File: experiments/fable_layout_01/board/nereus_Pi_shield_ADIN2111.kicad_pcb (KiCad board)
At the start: 6 copper layers, 138 parts, among them J1 Raspberry_Pi_2_3, J5 43650-0200, T1 74930000, T2 74930000, U1 ADIN2111BCPZ, U10 LMR51430YDDCR, U11 TPS26621DRCR, U2 AP22913CN4-7, U3 AP22913CN4-7, U4 INA232AIDDFR, U5 LMR51430YDDCR, U6 TPS62840YBGR, Y1 ABM11W-25.0000MHZ-6-K1Z-T3

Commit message: fable layout 01 M0b: J5 stays the JST GH (Nick); schematic copy unchanged, board rebuilt
Co-Authored-By: Claude Fable 5.1 <noreply@anthropic.com>
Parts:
- J5: value 43650-0200 -> SM02B-GHS-TB; footprint Connector_Molex:Molex_Micro-Fit_3.0_43650-0200_1x02_P3.00mm_Horizontal -> Connector_JST:JST_GH_SM02B-GHS-TB_1x02-1MP_P1.25mm_Horizontal

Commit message: fable layout 01 M1: outline, J1, holes, inserts with Sofar's ring copper, J5, envelopes; build pipeline
Co-Authored-By: Claude Fable 5.1 <noreply@anthropic.com>
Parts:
- J1, MP1, MP2, MP3, MP4: moved to B.Cu
- moved MTG3 173.9 mm to (-3.50, 61.5)
- moved L1 167.3 mm to (12.7, 44.2), turned to 90 degrees
- moved MTG1 160.4 mm to (-3.50, 3.50)
- moved MTG4 146.0 mm to (34.5, 61.5)
- moved MP4 144.7 mm to (-1.81, 21.4), turned to 176 degrees
- moved MP3 137.2 mm to (-1.81, 12.0), turned to 176 degrees
- moved J5 136.7 mm to (15.0, 61.8)
- moved MTG2 133.8 mm to (34.5, 3.50)
- moved MP2 121.8 mm to (-1.81, 53.0), turned to 176 degrees
- moved J1 119.0 mm to (25.2, 8.37), turned to 180 degrees
- moved MP1 112.0 mm to (-1.81, 43.6), turned to 176 degrees
- moved L2 66.2 mm to (12.7, 16.8), turned to 90 degrees
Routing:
- net /Top-Level Schematic/BM2_P: track 0.00 -> 11.6 mm, vias 0 -> 7
- net /Top-Level Schematic/BM2_N: track 0.00 -> 11.6 mm, vias 0 -> 7
- net /Top-Level Schematic/BM1_P: track 0.00 -> 11.6 mm, vias 0 -> 7
- net /Top-Level Schematic/BM1_N: track 0.00 -> 11.6 mm, vias 0 -> 7
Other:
- board outline added: 46 x 65 mm
- board text added: "L1 50 W envelope 15.5 x 15.5 (+2 mm clear)"
- board text added: "L2 50 W envelope 15.5 x 15.5 (+2 mm clear)"

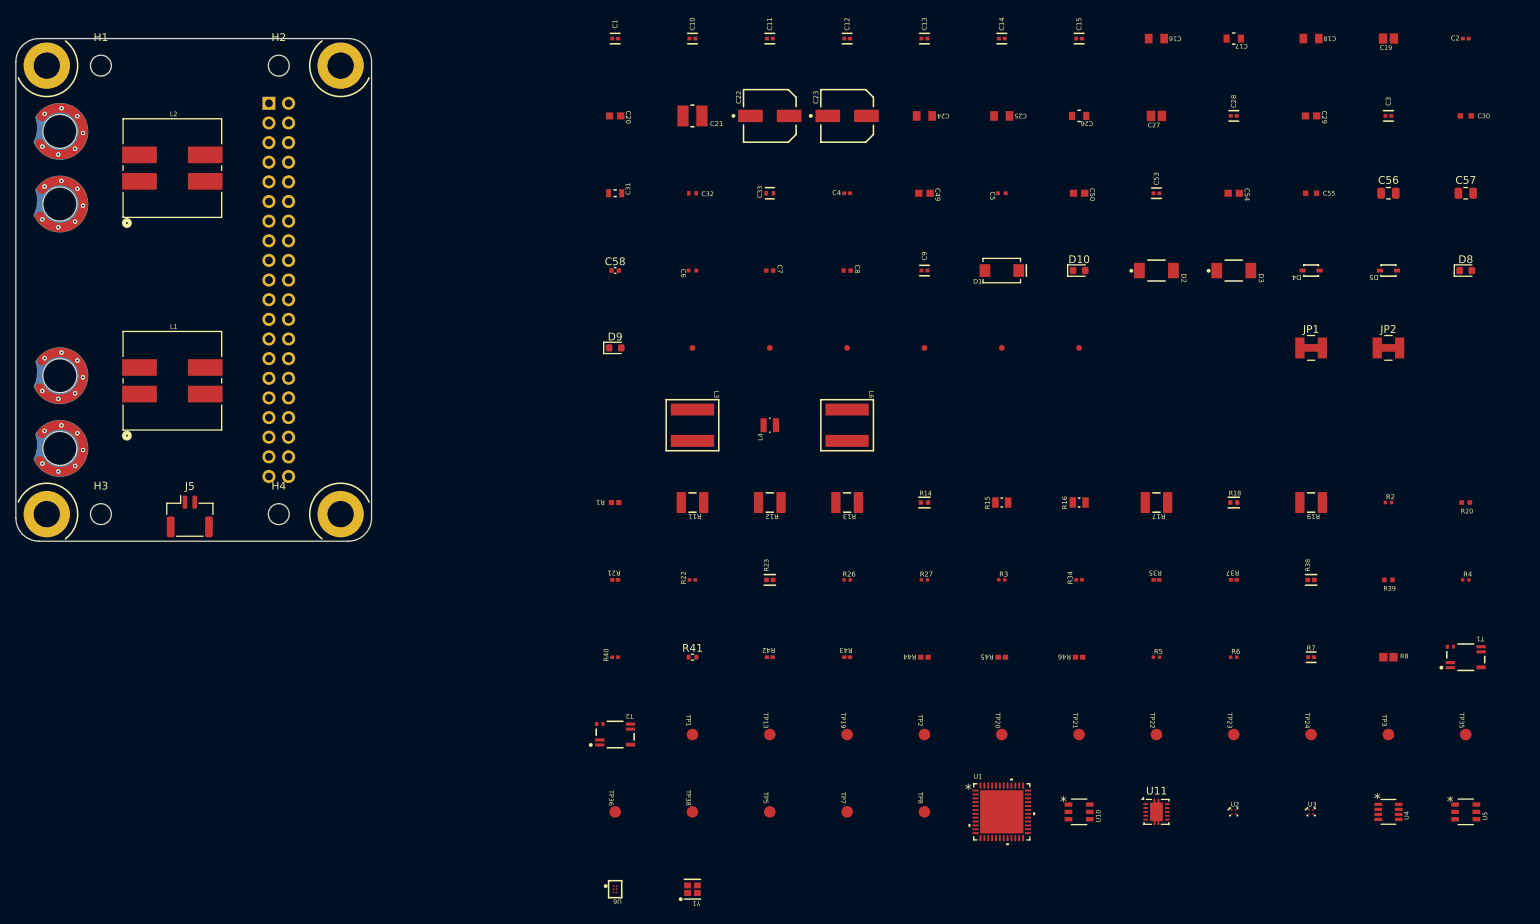
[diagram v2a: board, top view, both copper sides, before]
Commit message: fable layout 01 M2: all parts placed; rigid sub-blocks, transforms in blocks.json, heights table
Co-Authored-By: Claude Fable 5.1 <noreply@anthropic.com>
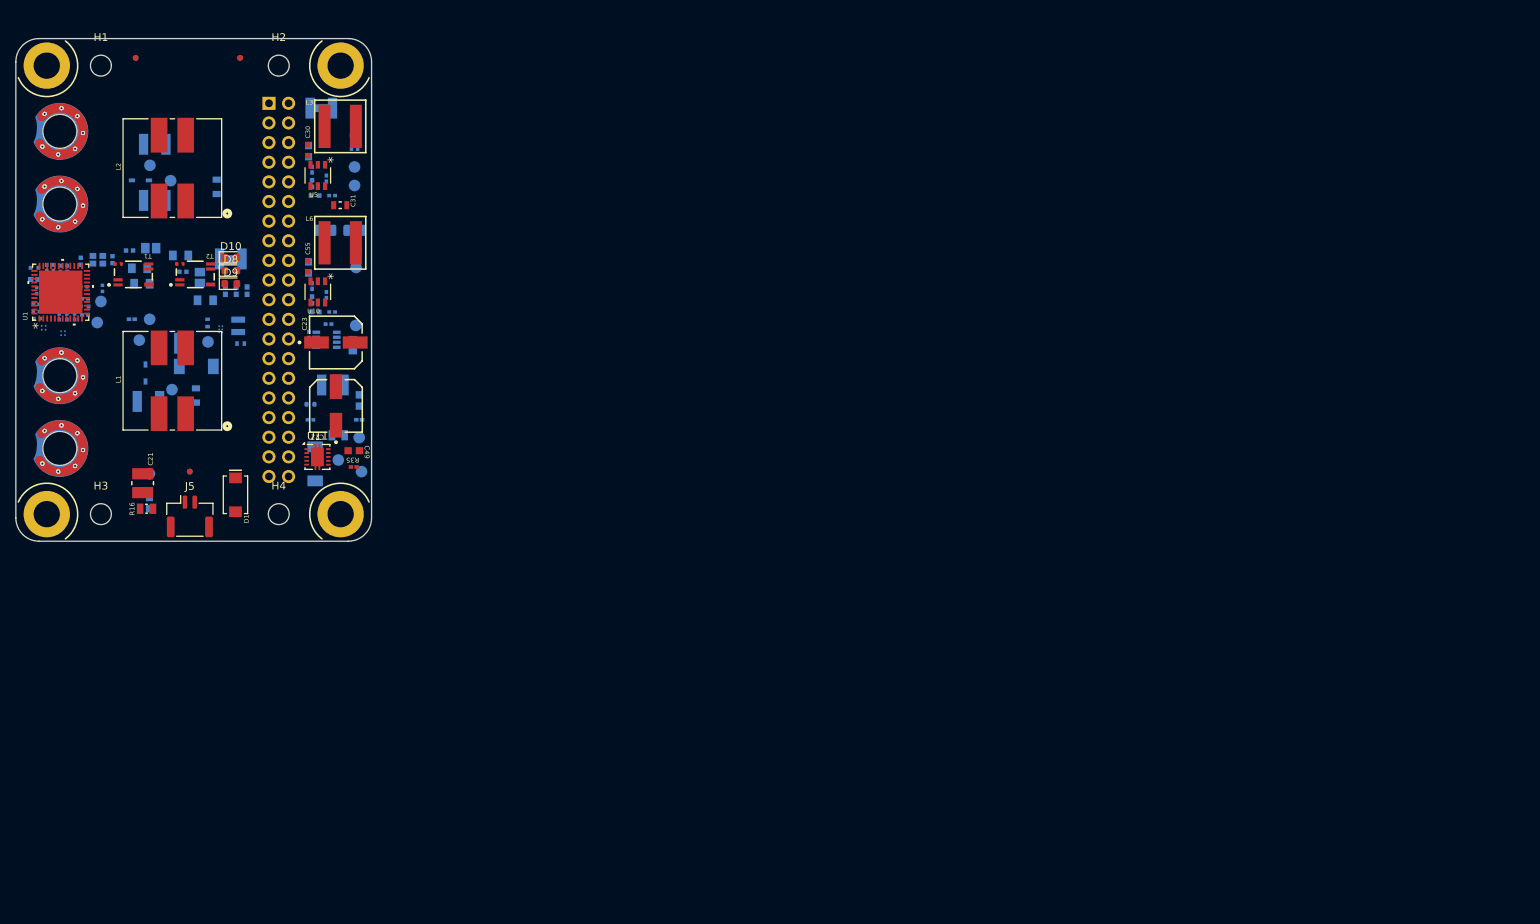
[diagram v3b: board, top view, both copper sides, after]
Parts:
- C1, C10, C11, C12, C13, C14, C15, C16, C17, C18, C19, C2, C20, C24, C25, C26, C27, C28, C29, C3, C32, C33, C4, C5, C50, C53, C54, C56, C57, C58, C6, C7, C8, C9, D2, D3, D4, D5, FID1, FID2, FID6, JP1, JP2, L4, R1, R11, R12, R13, R14, R15, R17, R18, R19, R2, R20, R21, R22, R23, R26, R27, R3, R34, R37, R38, R39, R4, R40, R41, R42, R43, R44, R45, R46, R5, R6, R7, R8, TP1, TP13, TP19, TP2, TP20, TP21, TP22, TP23, TP24, TP3, TP35, TP36, TP38, TP5, TP7, TP8, U2, U3, U4, U6, Y1: moved to B.Cu
- moved R4 188.1 mm to (-4.85, 35.3)
- moved C2 183.5 mm to (0.10, 36.0), turned to 90 degrees
- moved T1 179.3 mm to (7.70, 30.5)
- moved U3 175.4 mm to (-3.90, 37.4), turned to -90 degrees
- moved C3 172.9 mm to (-1.75, 29.8), turned to -90 degrees
- moved R2 171.0 mm to (1.30, 32.1), turned to 180 degrees
- moved U5 169.7 mm to (31.6, 17.7), turned to -90 degrees
- moved TP3 169.4 mm to (8.46, 39.0), turned to 180 degrees
- moved U2 163.6 mm to (-1.40, 38.1), turned to -90 degrees
- moved C19 162.3 mm to (9.95, 27.1), turned to 180 degrees
- moved R6 161.9 mm to (-4.80, 32.6), turned to -90 degrees
- moved D5 161.8 mm to (8.62, 18.3)
- moved D8 159.7 mm to (20.3, 30.0)
- moved R19 154.6 mm to (10.5, 20.9)
- moved C18 154.5 mm to (8.80, 31.7)
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
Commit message: fable layout 01 M3: block copper copied; blockcheck 1064/1064 matched, 0 extra
Co-Authored-By: Claude Fable 5.1 <noreply@anthropic.com>
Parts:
- moved R11 18.2 mm to (21.0, 58.0), turned to 90 degrees
- moved TP36 16.6 mm to (19.5, 62.3)
- moved C33 12.4 mm to (19.9, 48.9), turned to 0 degrees
- moved TP21 10.8 mm to (22.3, 48.9), turned to 180 degrees
- moved U6 9.75 mm to (20.7, 47.2), turned to 90 degrees
- moved L4 7.86 mm to (20.2, 45.0), turned to 0 degrees
- moved R26 7.73 mm to (37.0, 20.2)
- moved R27 7.73 mm to (37.0, 22.0)
- moved C32 5.27 mm to (22.6, 44.6), turned to -90 degrees
- moved C57 4.72 mm to (31.6, 25.2)
- moved C31 4.41 mm to (36.6, 17.7)
- moved R15 4.25 mm to (30.5, 49.2), turned to 90 degrees
- moved R41 4.00 mm to (30.7, 43.3)
- moved R34 4.00 mm to (30.6, 45.3)
- moved TP24 3.68 mm to (34.9, 22.4)
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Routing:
- net GND: track 0.00 -> 66.0 mm, vias 0 -> 60
- net VBUS: track 0.00 -> 31.5 mm, vias 0 -> 9
- net /Top-Level Schematic/BM2_P: track 11.6 -> 42.1 mm, vias 7 -> 12
- net 3V3: track 0.00 -> 28.5 mm, vias 0 -> 6
- net /Top-Level Schematic/BM1_P: track 11.6 -> 36.8 mm, vias 7 -> 12
- net /Top-Level Schematic/BM1_N: track 11.6 -> 36.1 mm, vias 7 -> 11
- net /Top-Level Schematic/ADIN_PWR: track 0.00 -> 19.4 mm, vias 0 -> 1
- net ADIN_VDDIO: track 0.00 -> 18.1 mm, vias 0 -> 4
- net /Top-Level Schematic/ADIN/ADIN_AVDD: track 0.00 -> 16.1 mm, vias 0 -> 5
- net /Top-Level Schematic/PoDL/Power Monitor/P_IN: track 0.00 -> 15.8 mm, vias 0 -> 4
- net /Top-Level Schematic/~{ADIN_RST}: track 0.00 -> 15.2 mm, vias 0 -> 1
- net /Top-Level Schematic/ADIN/ADIN_CLK25_REF: track 0.00 -> 14.0 mm, vias 0 -> 2
- net /Top-Level Schematic/BM2_N: track 11.6 -> 25.2 mm, vias 7 -> 10
- net /Top-Level Schematic/5V_PI: track 0.00 -> 12.7 mm, vias 0 -> 4
- net 1V8: track 0.00 -> 11.3 mm
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- added copper zone on F.Cu, net /Top-Level Schematic/5V_PI
- added copper zone on In4.Cu, net /Top-Level Schematic/ADIN/ADIN_AVDD
- added copper zone on F.Cu, net /Top-Level Schematic/Power Regulators/3V3_Buck_SW
- added copper zone on F.Cu, net /Top-Level Schematic/Power Regulators/5V_Buck_SW
- added copper zone on F.Cu, net 3V3
- added copper zone on In4.Cu, net ADIN_VDDIO
